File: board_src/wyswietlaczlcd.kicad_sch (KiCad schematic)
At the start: 5 parts, among them J19 Conn_02x07_Odd_Even, Q6 BC107

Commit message: wersja z FT232RN
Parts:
- removed Q6: BC107, OptoDevice:Osram_SFH3710, symbol Transistor_BJT:BC107
- removed R3: R, Resistor_SMD:R_0201_0603Metric, symbol Device:R
- added J7: Conn_01x16_Socket, Connector_PinSocket_2.54mm:PinSocket_1x16_P2.54mm_Vertical, symbol Connector:Conn_01x16_Socket
- added Q7: BC107, OptoDevice:Osram_SFH3710, symbol Transistor_BJT:BC107
- added R4: R, Resistor_SMD:R_1206_3216Metric, symbol Device:R
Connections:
- net +3.3V: now also J7.16 (Pin_16), J7.2 (Pin_2); no longer DS4.16 (K_1), DS4.2 (VDD)
- net BL: now also R4.2
- net D0: now also J7.7 (Pin_7); no longer DS4.7 (DB0)
- net D1: now also J7.8 (Pin_8); no longer DS4.8 (DB1)
- net D2: now also J7.9 (Pin_9); no longer DS4.9 (DB2)
- net D3: now also J7.10 (Pin_10); no longer DS4.10 (DB3)
- net D4: now also J7.11 (Pin_11); no longer DS4.11 (DB4)
- net D5: now also J7.12 (Pin_12); no longer DS4.12 (DB5)
- net D6: now also J7.13 (Pin_13); no longer DS4.13 (DB6)
- net D7: now also J7.14 (Pin_14); no longer DS4.14 (DB7)
- net E: now also J7.6 (Pin_6); no longer DS4.6 (E)
- net GND: now also J7.1 (Pin_1), Q7.1 (E); no longer DS4.1 (VSS)
- net RS: now also J7.4 (Pin_4); no longer DS4.4 (RS)
- net R/W: now also J7.5 (Pin_5); no longer DS4.5 (R/~{W})
- net at RV1.2: now also J7.3 (Pin_3); no longer DS4.3 (VO)
- new net: J7.15 (Pin_15), Q7.3 (C)
- new net: Q7.2 (B), R4.1
- no-connect marks 8 -> 24
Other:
- moved on the sheet: RV1

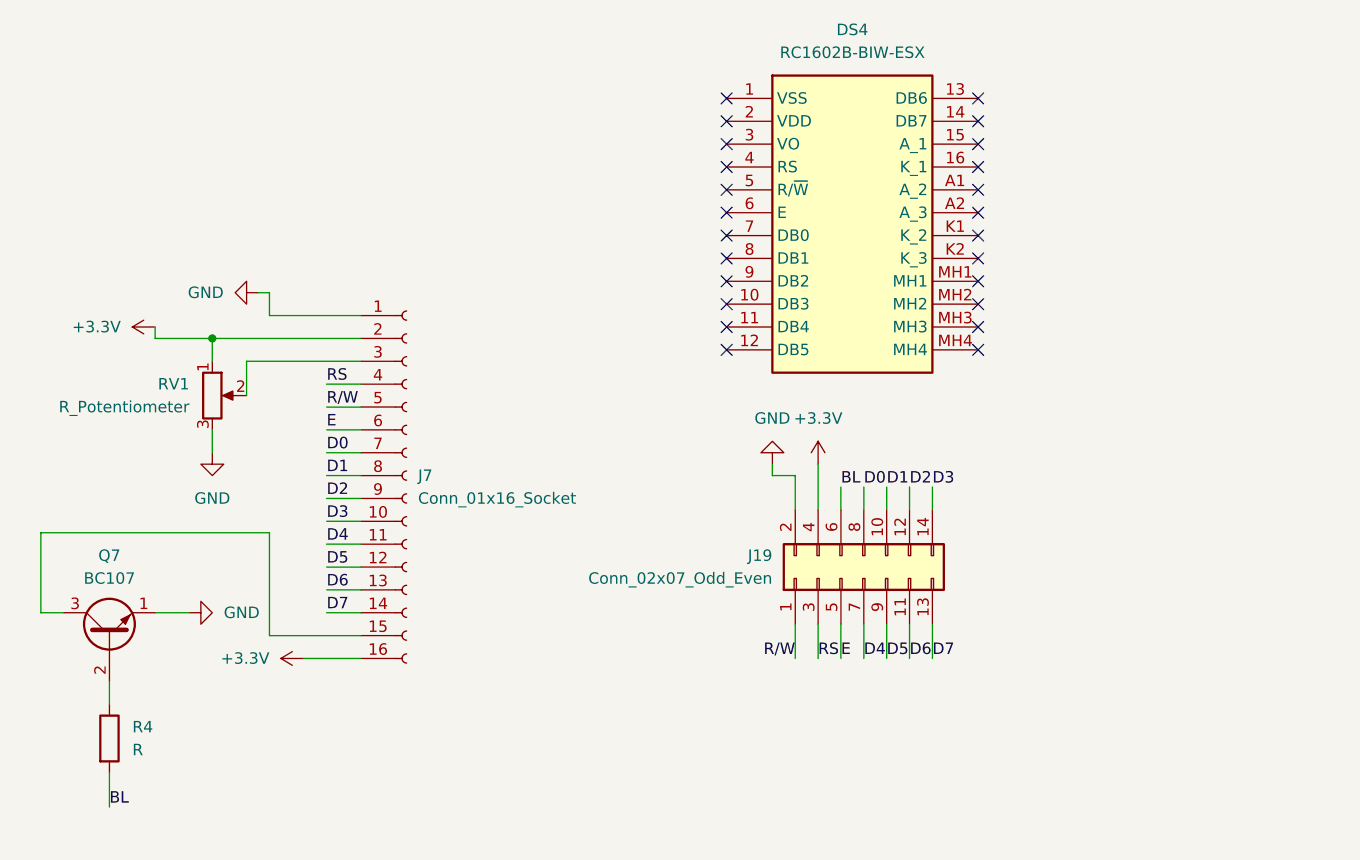
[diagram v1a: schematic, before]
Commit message: Wersja ze sciezkami miedzianymi
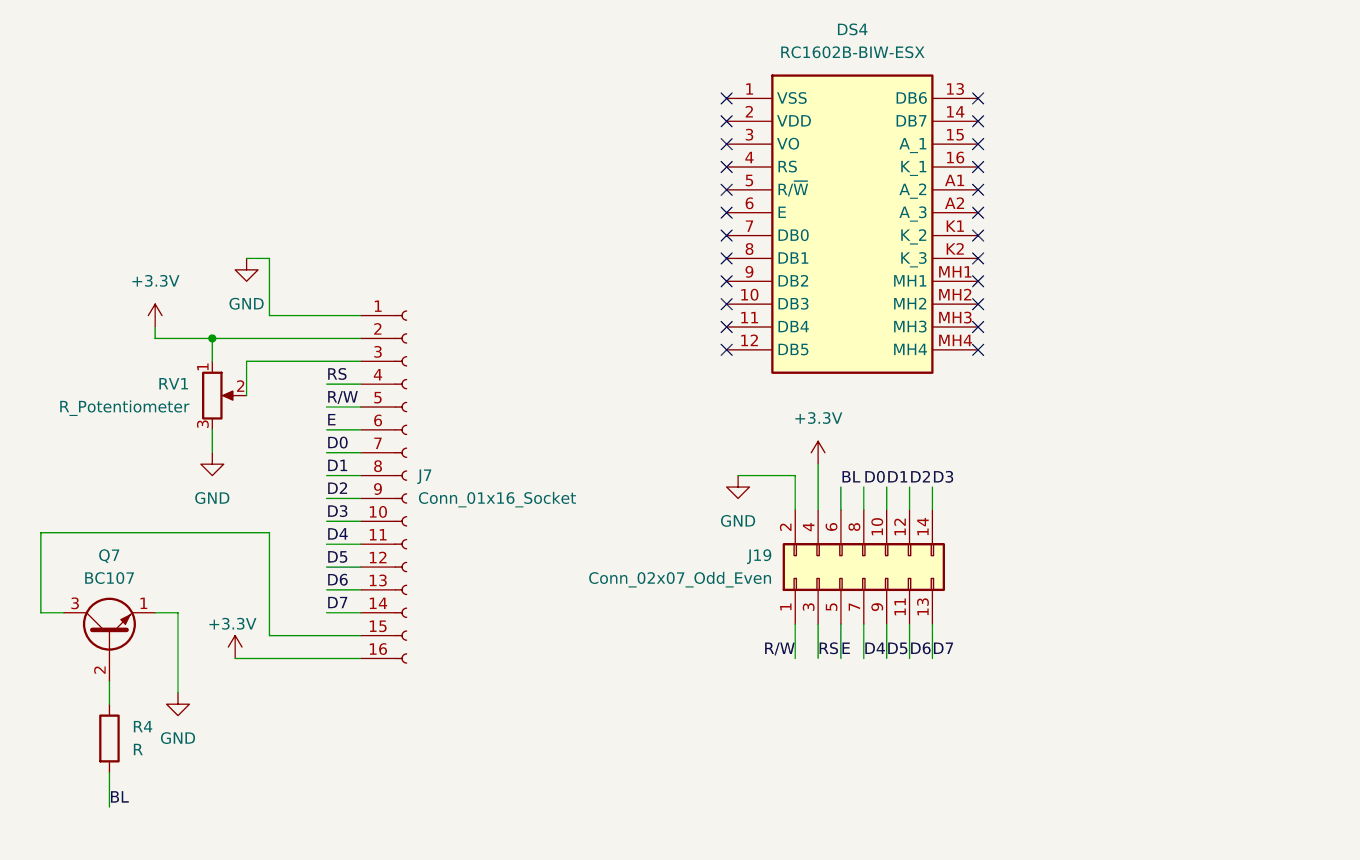
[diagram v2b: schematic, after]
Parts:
- Q7: footprint OptoDevice:Osram_SFH3710 -> Package_TO_SOT_SMD:SOT-23
- R4: footprint Resistor_SMD:R_1206_3216Metric -> Resistor_SMD:R_0603_1608Metric

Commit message: poprawione polaczenia diod i wartosci opornikow, aktualizacja niektorych elementow ze wzgledu na braki w magazynie
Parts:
- RV1: footprint Potentiometer_SMD:Potentiometer_Bourns_3314R-GM5_Vertical -> footprints:PT6KV251A2020
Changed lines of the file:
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@@
+			"AAAAAAAAAAAAAAAAAAAAAAAAAAAAAAAAAAAAAAAAAAAAAAAAAAAAAAAAAAAAAAAAAAAAAAAAAAAA"
+			"AAAAAAAAAAAAAAAAAAAAAAAAAAAAAAAAAAAAAAAAAAAAAAAAAAAAAAAAAAAAAAAAAAAAAAAAAAAA"
+			"AAAAAAAAAAAAAAAAAAAAAAAAAAAAAAAAAAAAAAAAAAAAAAAAAAAAAAAAAAAAAAAAAAAAAAAAAAAA"
+			"AAAAAAAAAAAAAAAAAAAAAAAAAAAAAAAAAAAAAAAAAAAAAAAAAAAAAAAAAAAAAAAAAAAAAAAAAAAA"
+			"AAAAAAAAAAAAAAAAAAAAAAAAAAAAAAAAAAAAAAAAAAAAAAAAAAAAAAAAAAAAAAAAAAAAAAAAAAAA"
+			"AAAAAAAAAAAAAAAAAAAAAAAAAAAAAAAAAAAAAAAAAAAAAAAAAAAAAAAAAAAAAAAAAAAAAAAAAAAA"
+			"AAAAAAAAAAAAAAAAAAAAAAAAAAAAAAAAAAAAAAAAAAAAAAAAAAAAAAAAAAAAAAAAAAAAAAAAAAAA"
+			"AAAAAAAAAAAAAAAAAAAAAAAAAAAAAAAAAAAAAAAAAAAAAAAAAAAAAAAAAAAAAAAAAAAAAAAAAAAA"
+			"AAAAAAAAAAAAAAAAAAAAAAAAAAAAAAAAAAAAAAAAAAAAAAAAAAAAAAAAAAAAAAAAAAAAAAAAAAAA"
+			"AAAAAAAAAAAAAAAAAAAAAAAAAAAAAAAAAAAAAAAAAAAAAAAAAAAAAAAAAAAAAAAAAAAAAAAAAAAA"
+			"AAAAAAAAAAAAAAAAAAAAAAAAAAAAAAAAAAAAAAAAAAAAAAAAAAAAAAAAAAAAAAAAAAAAAAAAAAAA"
+			"AAAAAAAAAAAAAAAAAAAAAAAAAAAAAAAAAAAAAAAAAAAAAAAAAAAAAAAAAAAAAAAAAAAAAAAAAAAA"
+			"AAAAAAAAAAAAAAAAAAAAAAAAAAAAAAAAAAAAAAAAAAAAAAAAAAAAAAAAAAAAAAAAAAAAAAAAAAAA"
+			"AAAAAAAAAAAAAAAAAAAAAAAAAAAAAAAAAAAAAAAAAAAAAAAAAAAAAAAAAAAAAAAAAAAAAAAAAAAA"
+			"AAAAAAAAAAAAAAAAAAAAAAAAAAAAAAAAAAAAAAAAAAAAAAAAAAAAAAAAAAAAAAAAAAAAAAAAAAAA"
+			"AAAAAAAAAAAAAAAAAAAAAAAAAAAAAAAAAAAAAAAAAAAAAAAAAAAAAAAAAAAAAAAAAAAAAAAAAAAA"
+			"AAAAAAAAAAAAAAAAAAAAAAAAAAAAAAAAAAAAAAAAAAAAAAAAAAAAAAAAAAAAAAAAAAAAAAAAAAAA"
+			"AAAAAAAAAAAAAAAAAAAAAAAAAAAAAAAAAAAAAAAAAAAAAAAAAAAAAAAAAAAAAAAAAAAAAAAAAAAA"
 			"AAAAAAAAAAAAAAAAAAAAAAAAAAAAAAAAAAAAAAAAAAAAAAAAAAAAAAAAAAAAAAAAAAAAAAAAAAAA"
 			"AAAAAAAAAAAAAAAAAAAAAAAAAAAAAAAAAAAAAAAAAAAAAAAAAAAAAAAAAAAAAAAAAAAAAAAAAAAA"
@@
 			)
 		)
-		(property "Footprint" "Potentiometer_SMD:Potentiometer_Bourns_3314R-GM5_Vertical"
+		(property "Footprint" "footprints:PT6KV251A2020"
 			(at 58.42 60.96 0)
 			(effects

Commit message: najnowsza wersja
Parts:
- R4: value R -> 4.7k
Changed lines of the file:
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@@
 			)
 		)
-		(property "Value" "R"
+		(property "Value" "4.7k"
 			(at 49.53 100.3299 0)
 			(effects

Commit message: finalna wersja, naniesione poprawki
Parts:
- removed DS4: RC1602B-BIW-ESX, footprints:RC1602BBIWESX, symbol RC1602B-BIW-ESX:RC1602B-BIW-ESX
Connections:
- no-connect marks 24 -> 0
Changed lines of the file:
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@@
 		(color 0 0 0 0)
-	)
-	(no_connect
-		(at 115.57 50.8)
-	)
-	(no_connect
-		(at 115.57 53.34)
-	)
-	(no_connect
-		(at 143.51 38.1)
-	)
-	(no_connect
-		(at 143.51 43.18)
-	)
-	(no_connect
-		(at 115.57 38.1)
-	)
-	(no_connect
-		(at 143.51 27.94)
-	)
-	(no_connect
-		(at 115.57 43.18)
-	)
-	(no_connect
-		(at 143.51 48.26)
-	)
-	(no_connect
-		(at 143.51 55.88)
-	)
-	(no_connect
-		(at 143.51 30.48)
-	)
-	(no_connect
-		(at 115.57 45.72)
-	)
-	(no_connect
-		(at 115.57 48.26)
-	)
-	(no_connect
-		(at 115.57 33.02)
-	)
-	(no_connect
-		(at 115.57 30.48)
-	)
-	(no_connect
-		(at 143.51 45.72)
-	)
-	(no_connect
-		(at 115.57 35.56)
-	)
-	(no_connect
-		(at 143.51 35.56)
-	)
-	(no_connect
-		(at 115.57 55.88)
-	)
-	(no_connect
-		(at 143.51 40.64)
-	)
-	(no_connect
-		(at 143.51 50.8)
-	)
-	(no_connect
-		(at 143.51 33.02)
-	)
-	(no_connect
-		(at 115.57 27.94)
-	)
-	(no_connect
-		(at 115.57 40.64)
-	)
-	(no_connect
-		(at 143.51 53.34)
 	)
 	(wire
@@
 					(unit 1)
 				)
-			)
-		)
-	)
-	(symbol
-		(lib_id "RC1602B-BIW-ESX:RC1602B-BIW-ESX")
-		(at 115.57 27.94 0)
-		(unit 1)
-		(exclude_from_sim no)
-		(in_bom yes)
-		(on_board yes)
-		(dnp no)
-		(fields_autoplaced yes)
-		(property "Reference" "DS4"
-			(at 129.54 20.32 0)
-			(effects
-				(font
-					(size 1.27 1.27)
-				)
-			)
-		)
-		(property "Value" "RC1602B-BIW-ESX"
-			(at 129.54 22.86 0)
-			(effects
-				(font
-					(size 1.27 1.27)
-				)
-			)
-		)
-		(property "Footprint" "footprints:RC1602BBIWESX"
-			(at 139.7 122.86 0)
-			(effects
-				(font
-					(size 1.27 1.27)
-				)
-				(justify left top)
-				(hide yes)
-			)
-		)
-		(property "Datasheet" "https://www.tme.eu/Document/53481d6ef60900b7bb1011c164e7f0a0/rc1602b-biw-esx.pdf"
-			(at 139.7 222.86 0)
-			(effects
-				(font
-					(size 1.27 1.27)
-				)
-				(justify left top)
-				(hide yes)
-			)
-		)
-		(property "Description" "Display: LCD; alphanumeric; STN Negative; 16x2; blue; LED; PIN: 16"
-			(at 115.57 27.94 0)
-			(effects
-				(font
-					(size 1.27 1.27)
-				)
-				(hide yes)
-			)
-		)
-		(property "Height" "10.2"
-			(at 139.7 422.86 0)
-			(effects
-				(font
-					(size 1.27 1.27)
-				)
-				(justify left top)
-				(hide yes)
-			)
-		)
-		(property "TME Electronic Components Part Number" ""
-			(at 139.7 522.86 0)
-			(effects
-				(font
-					(size 1.27 1.27)
-				)
-				(justify left top)
-				(hide yes)
-			)
-		)
-		(property "TME Electronic Components Price/Stock" ""
-			(at 139.7 622.86 0)
-			(effects
-				(font
-					(size 1.27 1.27)
-				)
-				(justify left top)
-				(hide yes)
-			)
-		)
-		(property "Manufacturer_Name" "RAYSTAR"
-			(at 139.7 722.86 0)
-			(effects
-				(font
-					(size 1.27 1.27)
-				)
-				(justify left top)
-				(hide yes)
-			)
-		)
-		(property "Manufacturer_Part_Number" "RC1602B-BIW-ESX"
-			(at 139.7 822.86 0)
-			(effects
-				(font
-					(size 1.27 1.27)
-				)
-				(justify left top)
-				(hide yes)
-			)
-		)
-		(pin "K2"
-		)
-		(pin "K1"
-		)
-		(pin "MH1"
-		)
-		(pin "A2"
-		)
-		(pin "MH4"
-		)
-		(pin "MH3"
-		)
-		(pin "MH2"
-		)
-		(pin "1"
-		)
-		(pin "5"
-		)
-		(pin "7"
-		)
-		(pin "6"
-		)
-		(pin "13"
-		)
-		(pin "14"
-		)
-		(pin "15"
-		)
-		(pin "2"
-		)
-		(pin "3"
-		)
-		(pin "16"
-		)
-		(pin "A1"
-		)
-		(pin "10"
-		)
-		(pin "8"
-		)
-		(pin "9"
-		)
-		(pin "11"
-		)
-		(pin "12"
-		)
-		(pin "4"
-		)
-		(instances
-			(project ""
-				(path "/772e9f49-cfcf-4cf6-843d-0684684f2d4b/99f2b7c2-bf4b-48af-983c-5ee0acdebe2a"
-					(reference "DS4")
-					(unit 1)
-				)

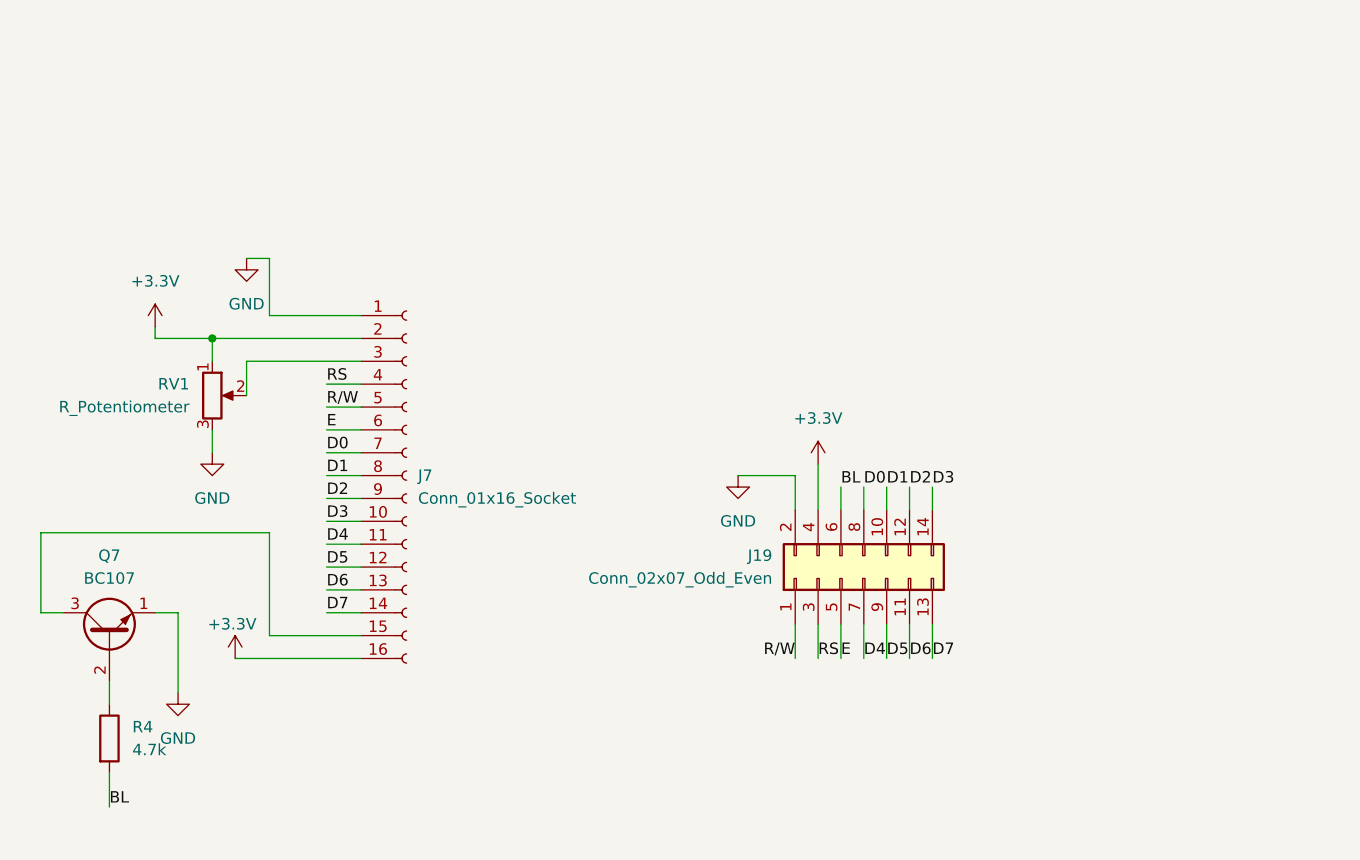
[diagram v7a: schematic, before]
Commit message: Poprawki w schematach. Rozpoczęte korekty płytki
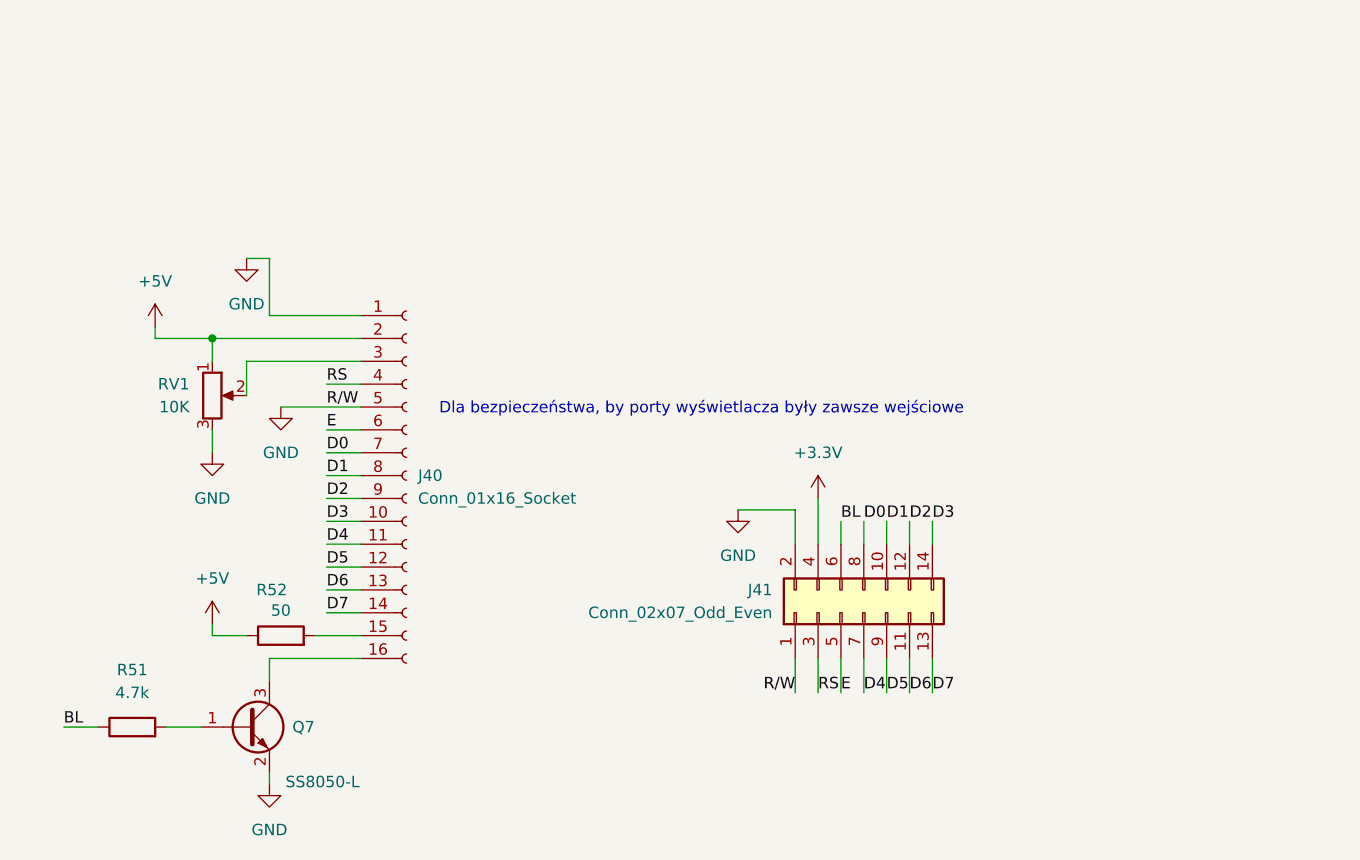
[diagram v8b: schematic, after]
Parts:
- removed Q7: BC107, Package_TO_SOT_SMD:SOT-23, symbol Transistor_BJT:BC107
- added Q7: SS8050-L, Package_TO_SOT_SMD:SOT-23_Handsoldering, symbol Transistor_BJT:SS8050
- added R52: 50, Resistor_SMD:R_0603_1608Metric_Pad0.98x0.95mm_HandSolder, symbol Device:R
- J40: renamed from J7; footprint Connector_PinSocket_2.54mm:PinSocket_1x16_P2.54mm_Vertical -> Connector_PinHeader_2.54mm:PinHeader_1x01_P2.54mm_Vertical
- J41: renamed from J19; footprint Connector_PinHeader_2.54mm:PinHeader_2x07_P2.54mm_Vertical -> Connector_PinHeader_2.54mm:PinHeader_1x01_P2.54mm_Vertical
- R51: renamed from R4; footprint Resistor_SMD:R_0603_1608Metric -> Resistor_SMD:R_0603_1608Metric_Pad0.98x0.95mm_HandSolder
- RV1: value R_Potentiometer -> 10K
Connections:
- net R/W is gone; now on net GND: J40.5 (Pin_5), J41.1 (Pin_1)
- net +3.3V: no longer J40.16 (Pin_16), J40.2 (Pin_2), RV1.1
- net BL: now also R51.1; no longer R51.2
- net GND: now also Q7.2 (E)
- net at J40.15 (Pin_15): now also R52.2
- new net: J40.16 (Pin_16), Q7.3 (C)
- new net: Q7.1 (B), R51.2
- new net +5V: J40.2 (Pin_2), R52.1, RV1.1
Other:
- note added: "Dla bezpieczeństwa, by porty wyświetlacza były zawsze wejściowe"
- moved on the sheet: J41, R51
